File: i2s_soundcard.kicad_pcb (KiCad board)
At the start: 4 copper layers, 83.1 x 50 mm, 21 parts, among them J1 Conn_01x08, J2 Conn_01x06, J3 Conn_01x05, J4 Conn_01x11, J5 Conn_01x04, U1 TLV320AIC3104IRHBT, U2 FSA2275UMX, U3 TPA2006D1DRBR, U4 FSA2275UMX, U5 TPA2006D1DRBR, U6 TLV7111830DSER, U7 TPD4E02B04DQAR, U8 TPD4E02B04DQAR

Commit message: fill in rest of in2 with ground fill
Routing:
- net /vbat: track 25.9 -> 27.5 mm
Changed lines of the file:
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@@
     (thickness 1)
     (drawings 61)
-    (tracks 443)
+    (tracks 445)
     (zones 0)
     (modules 21)
@@
   (segment (start 159.054802 97.3) (end 161.954802 100.2) (width 0.19) (layer In2.Cu) (net 33))
   (segment (start 158.8 97.3) (end 159.054802 97.3) (width 0.19) (layer In2.Cu) (net 33))
+  (segment (start 166.2 100.2) (end 167.6 100.2) (width 0.19) (layer In2.Cu) (net 33))
+  (segment (start 167.6 100.2) (end 167.7 100.1) (width 0.19) (layer In2.Cu) (net 33))
   (segment (start 165.027989 100.027989) (end 166.2 101.2) (width 0.19) (layer F.Cu) (net 34))
   (segment (start 165.027989 96.585908) (end 165.027989 100.027989) (width 0.19) (layer F.Cu) (net 34))
@@
     (polygon
       (pts
-        (xy 173.275 76.6) (xy 169 80.875) (xy 168.5 106.9) (xy 164.5 106.2) (xy 164.3375 94.7375)
-        (xy 165.6 82.1) (xy 166.4 81.2) (xy 167.3 73.3) (xy 164.3 70.1) (xy 161.3 77.8)
-        (xy 103.3875 77.8) (xy 86.1 72.3) (xy 86.15 56) (xy 173.275 56)
+        (xy 173.275 76.6) (xy 169 80.875) (xy 168.509375 100.5) (xy 166.290625 100.45) (xy 166.3 95)
+        (xy 166.7 87) (xy 165.7 86.2) (xy 165.6 82.1) (xy 166.4 81.2) (xy 167.3 73.3)
+        (xy 164.3 70.1) (xy 161.3 77.8) (xy 103.3875 77.8) (xy 86.1 72.3) (xy 86.15 56)
+        (xy 173.275 56)
       )
     )
@@
     (polygon
       (pts
-        (xy 164.4 70.5) (xy 167 73.4) (xy 166.2 81) (xy 160.65 87.35) (xy 160.2 90.7)
-        (xy 161.3 93.6) (xy 161.3 95.4) (xy 159.35 95.4) (xy 159.5 95.9) (xy 157.7 94.1)
-        (xy 158.9 85.8) (xy 164.3 80.3) (xy 163.4 73)
+        (xy 164.4 70.5) (xy 167 73.4) (xy 166.2 81) (xy 165.3 82) (xy 165.5 86.3)
+        (xy 166.4 87.2) (xy 166 95.7) (xy 166 100.7) (xy 168.6 100.9) (xy 171.575 111.2)
+        (xy 153.4 108.7875) (xy 152.9 84.125) (xy 162.3 78.05) (xy 163.4 73)
       )
     )

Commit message: Capitalize net names
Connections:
- net /LOL+ renamed /LOL_P
- net /LOL- renamed /LOL_N
- net /LOR+ renamed /LOR_P
- net /LOR- renamed /LOR_N
- net /bclk renamed /BCLK
- net /din renamed /DIN
- net /dout renamed /DOUT
- net /en1 renamed /EN1
- net /en2 renamed /EN2
- net /intmic+ renamed /INTMIC_P
- net /intmic- renamed /INTMIC_N
- net /iovdd renamed /IOVDD
- net /mclk renamed /MCLK
- net /mute renamed /MUTE
- net /reset renamed /RESET
- net /ring1 renamed /RING1
- net /ring2 renamed /RING2
- net /ring2_again renamed /RING2_AGAIN
- net /sca renamed /SCA
- net /scl renamed /SCL
- net /sel renamed /SEL
- net /sleeve renamed /SLEEVE
- net /tip renamed /TIP
- net /v1.8 renamed /VCC1.8
- net /v3.3 renamed /VCC3.3
- net /vbat renamed /VBAT_3.7
- net /wclk renamed /WCLK
- net /~shutdown renamed /~SHUTDOWN
- net Net-(J1-Pad7) renamed /DETECT?

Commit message: Lots of schematic cleanup and board tweaking
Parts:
- added C10: 10uF, Capacitor_SMD:C_0402_1005Metric, B.Cu at (163.7, 91.7)
- added C11: 100nF, Capacitor_SMD:C_0402_1005Metric, B.Cu at (165.7, 91.7)
- added C8: 0.1uF, Capacitor_SMD:C_0402_1005Metric, B.Cu at (161.5, 92.0)
- added C9: 220nF, Capacitor_SMD:C_0402_1005Metric, B.Cu at (162.3, 86.5)
- C4: value 1uF -> 10uF; moved to B.Cu
- C5: value 1uF -> 22uF; moved to B.Cu
- U6: moved to B.Cu
- moved J4 4.22 mm to (166.2, 103.1)
- moved U6 3.28 mm to (163.1, 94.0), turned to 180 degrees
- moved C2 2.08 mm to (156.3, 97.5), turned to 270 degrees
- moved C4 1.84 mm to (160.9, 90.0), turned to 270 degrees
- moved C5 1.58 mm to (160.9, 88.0)
- moved U8 0.76 mm to (164.0, 82.6)
- moved U2 0.50 mm to (158.0, 98.1), turned to 0 degrees
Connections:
- net /VCC3.3 renamed /VCC3.0
- J3 pad 3: /EN2 -> /EN1
- J3 pad 5: /EN1 -> /EN2
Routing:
- net /SEL: track 24.5 -> 16.9 mm
- net /MUTE: track 23.6 -> 17.0 mm
- net /RESET: track 22.5 -> 16.0 mm
- net /VBAT_3.7: track 27.5 -> 33.1 mm
- net /spkr_amp_left/SLO+: track 96.6 -> 91.2 mm
- net /SCA: track 17.9 -> 12.7 mm
- net /SCL: track 16.8 -> 12.0 mm
- net /~SHUTDOWN: track 106.9 -> 102.5 mm
- net /DOUT: track 16.3 -> 11.9 mm
- net GND: track 47.8 -> 43.8 mm, vias 24 -> 23
- net /EN2: track 4.26 -> 8.18 mm
- net /DIN: track 16.1 -> 12.2 mm
- net /LOR_N: track 2.64 -> 6.43 mm
- net /VCC1.8: track 7.85 -> 4.22 mm, vias 2 -> 1
- net /WCLK: track 15.9 -> 12.6 mm
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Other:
- board size 83.1 x 50 mm -> 83.1 x 46.3 mm

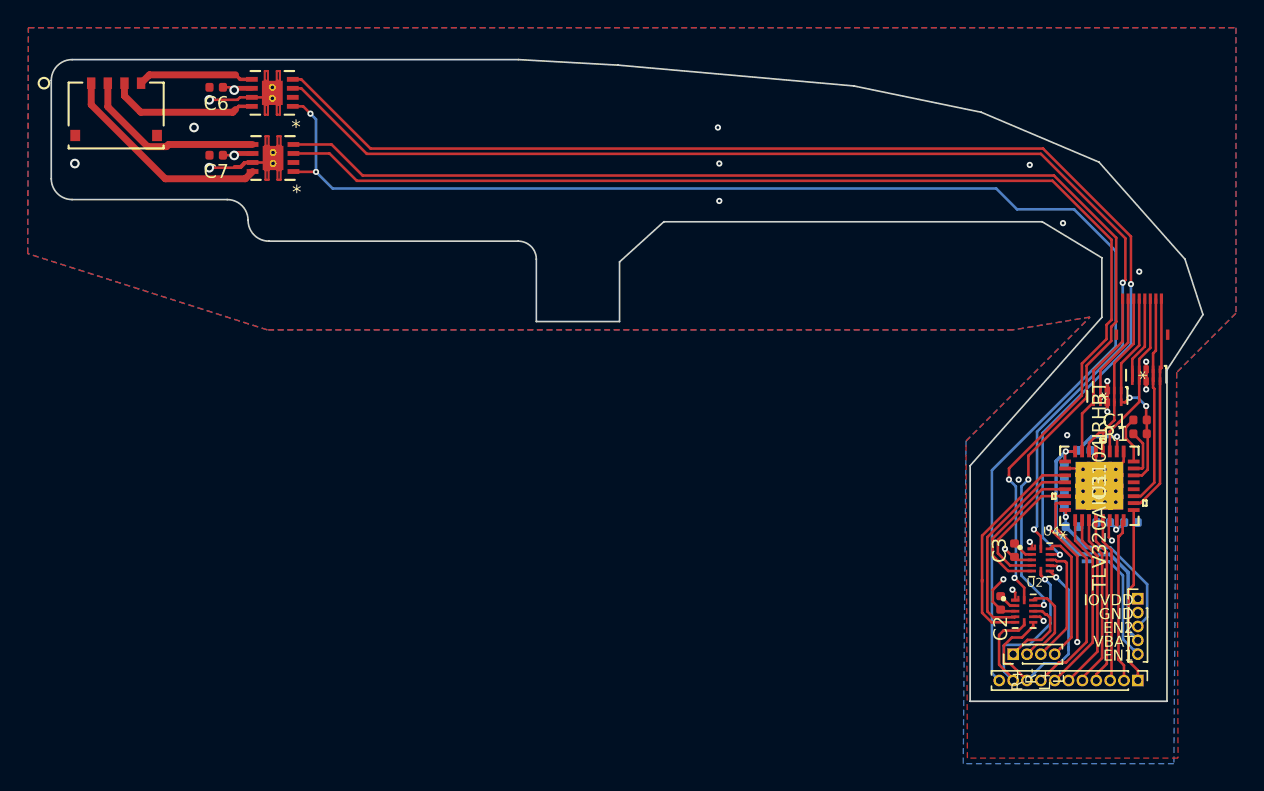
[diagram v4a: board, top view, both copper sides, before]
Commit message: AC-couple headphone outputs. This frees up HPRCOM and HPLCOM, which I can use for line outputs, since the dock line out is single-ended anyway.
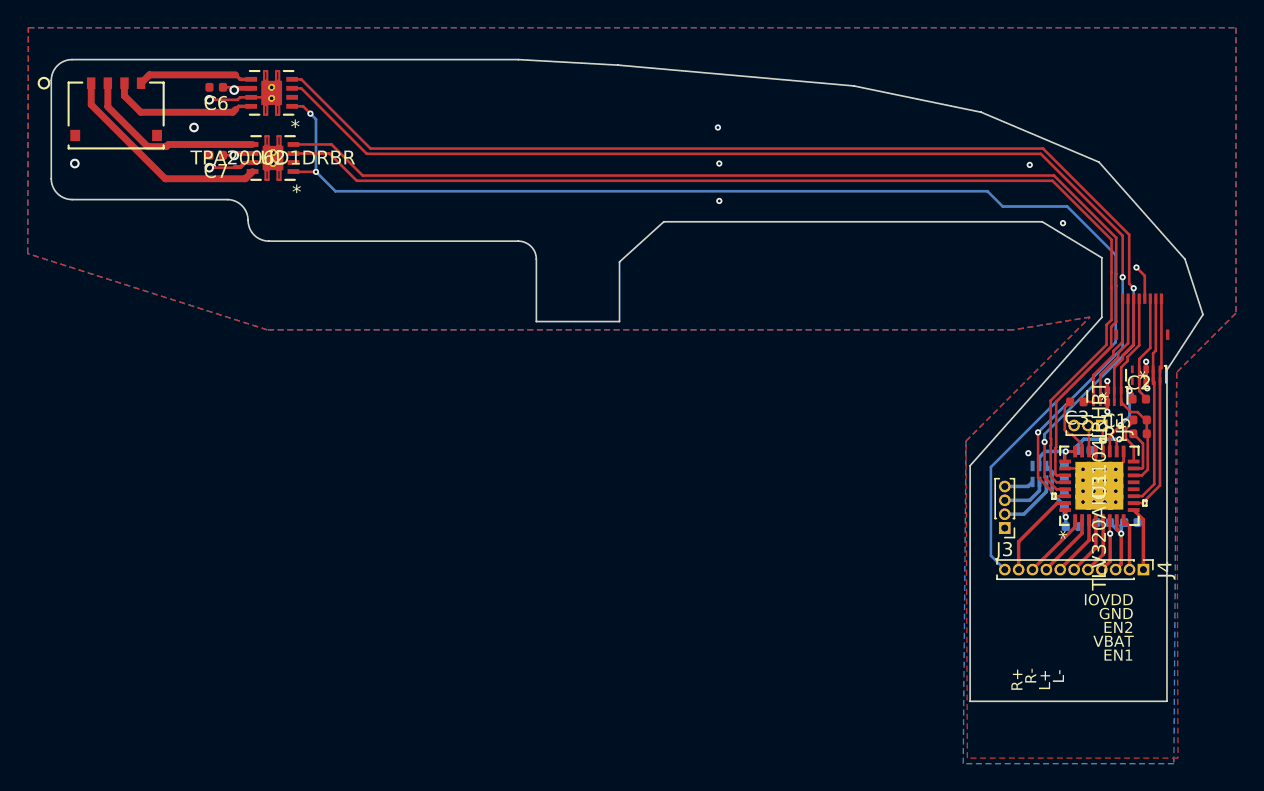
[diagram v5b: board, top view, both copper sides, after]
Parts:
- removed U4: FSA2275UMX, footprints:FSA2275
- removed U5: TPA2006D1DRBR, footprints:TPA2006D1DRBR
- C2, C3: value 0.1uF -> C
- J3: value Conn_01x05 -> Conn_01x04; footprint Connector_PinHeader_1.00mm:PinHeader_1x05_P1.00mm_Vertical -> Connector_PinHeader_1.00mm:PinHeader_1x04_P1.00mm_Vertical
- J5: value Conn_01x04 -> Conn_01x03; footprint Connector_PinHeader_1.00mm:PinHeader_1x04_P1.00mm_Vertical -> Connector_PinHeader_1.00mm:PinHeader_1x03_P1.00mm_Vertical
- U2: value FSA2275UMX -> TPA2006D1DRBR; footprint footprints:FSA2275 -> footprints:TPA2006D1DRBR
- moved U2 63.3 mm to (103.8, 65.4), turned to 180 degrees
- moved C2 17.8 mm to (166.3, 82.8), turned to 0 degrees
- moved J5 17.7 mm to (163.6, 84.7), turned to 270 degrees
- moved C3 11.6 mm to (161.8, 83.0), turned to 180 degrees
- moved J3 10.9 mm to (156.6, 92.1), turned to 180 degrees
- moved J4 8.01 mm to (166.6, 95.1)
- moved U6 7.05 mm to (159.1, 88.2), turned to 90 degrees
- moved U3 4.70 mm to (103.7, 60.7)
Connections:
- C2 pad 2: GND -> /TIP
- C3 pad 1: Net-(C3-Pad1) -> /RING1
- C3 pad 2: GND -> Net-(C3-Pad2)
- J1 pad 4: /RING2 -> GND
- J3 pad 1: /IOVDD -> GND
- J3 pad 2: GND -> /EN1
- J3 pad 3: /EN1 -> /VBAT_3.7
- J3 pad 4: /VBAT_3.7 -> /EN2
- J4 pad 10: /SEL -> /RESET
- J4 pad 3: /DOUT -> /IOVDD
- J4 pad 4: /DIN -> GND
- J4 pad 5: /WCLK -> /DOUT
- J4 pad 6: /BCLK -> /DIN
- J4 pad 7: /MCLK -> /WCLK
- J4 pad 8: /RESET -> /BCLK
- J4 pad 9: /MUTE -> /MCLK
- J5 pad 1: /LOR_P -> /LOL
- J5 pad 2: /LOR_N -> /LOR
- J5 pad 3: /LOL_P -> GND
- U1 pad 12: Net-(U1-Pad12) -> (no net)
- U1 pad 13: Net-(U1-Pad13) -> (no net)
- U1 pad 19: /TIP -> Net-(C2-Pad1)
- U1 pad 20: /RING2_AGAIN -> /LOL
- U1 pad 22: /RING2_AGAIN -> /LOR
- U1 pad 23: /RING1 -> Net-(C3-Pad2)
- U2 pad 1: /VBAT_3.7 -> /~SHUTDOWN
- U2 pad 2: Net-(C2-Pad1) -> (no net)
- U2 pad 3: GND -> /spkr_amp_left/LINEIN-
- U2 pad 4: /spkr_amp_left/LINEIN- -> /spkr_amp_left/LINEIN+
- U2 pad 5: /spkr_amp_left/LINEIN+ -> /spkr_amp_left/SPKR-
- U2 pad 6: /SEL -> /VBAT_3.7
- U2 pad 7: /MUTE -> GND
- U2 pad 8: GND -> /spkr_amp_left/SPKR+
- U2 pad 9: /LOR_P -> GND
- U3 pad 2: Net-(U3-Pad2) -> (no net)
- U3 pad 3: /spkr_amp_left/SLO+ -> /spkr_amp_right/LINEIN-
- U3 pad 4: /spkr_amp_left/SLO- -> /spkr_amp_right/LINEIN+
- U3 pad 5: /spkr_amp_left/SPKR- -> /spkr_amp_right/SPKR-
- U3 pad 8: /spkr_amp_left/SPKR+ -> /spkr_amp_right/SPKR+
- U7 pad 5: /RING2 -> (no net)
- U7 pad 6: /RING2 -> (no net)
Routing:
- net /spkr_amp_left/SLO-: track 92.9 -> 0.00 mm, vias 2 -> 0
- net /spkr_amp_right/SLO-: track 92.0 -> 0.00 mm, vias 2 -> 0
- net /spkr_amp_left/SLO+: track 91.2 -> 0.00 mm, vias 2 -> 0
- net /spkr_amp_right/SLO+: track 89.9 -> 0.00 mm, vias 2 -> 0
- net /spkr_amp_right/LINEIN-: track 9.93 -> 86.8 mm, vias 0 -> 2
- net /spkr_amp_right/LINEIN+: track 11.2 -> 87.1 mm, vias 0 -> 2
- net /spkr_amp_left/LINEIN-: track 14.8 -> 81.7 mm
- net /spkr_amp_left/LINEIN+: track 16.2 -> 81.8 mm
- net /VBAT_3.7: track 33.1 -> 7.85 mm, vias 4 -> 2
- net /MUTE: track 17.0 -> 0.00 mm, vias 1 -> 0
- net /SEL: track 16.9 -> 0.00 mm, vias 1 -> 0
- net GND: track 43.8 -> 33.3 mm, vias 23 -> 16
- net /RESET: track 16.0 -> 6.52 mm
- net /LOL_N: track 9.49 -> 0.00 mm
- net /LOL_P: track 8.67 -> 0.00 mm
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
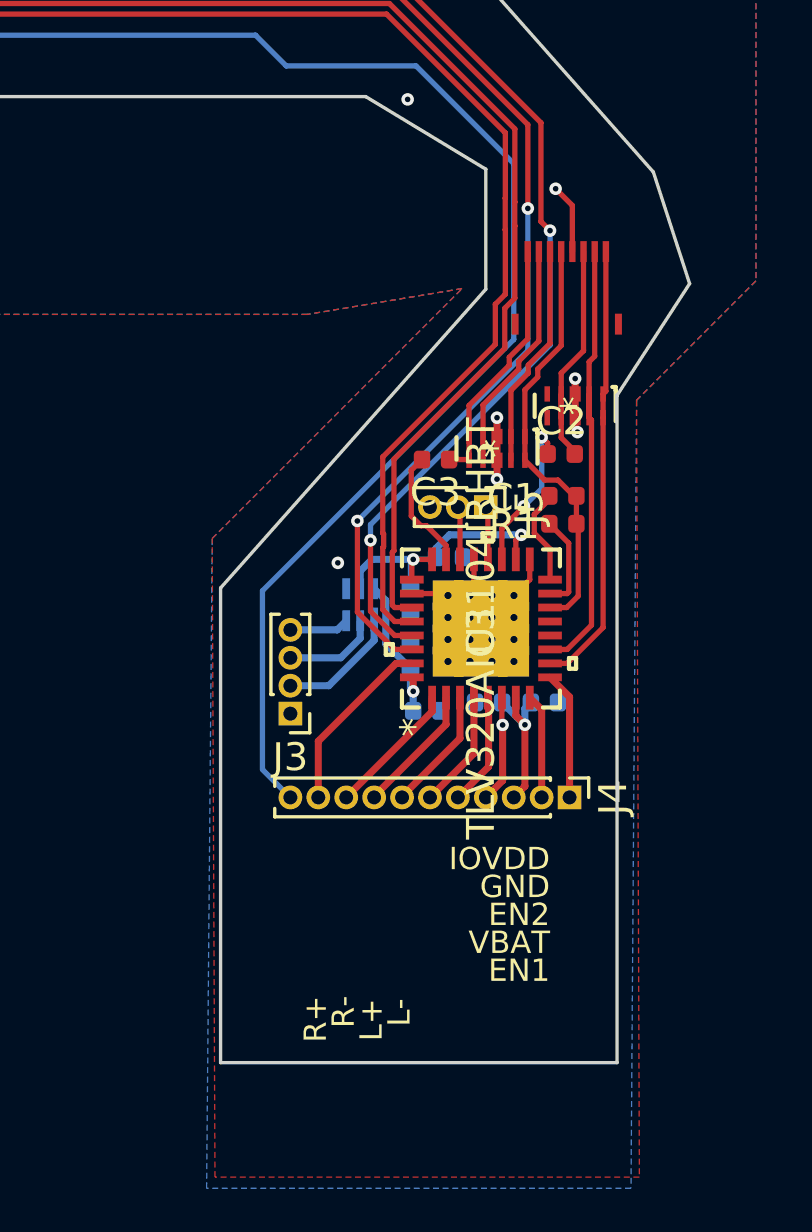
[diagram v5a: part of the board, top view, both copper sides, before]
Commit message: Shrink board
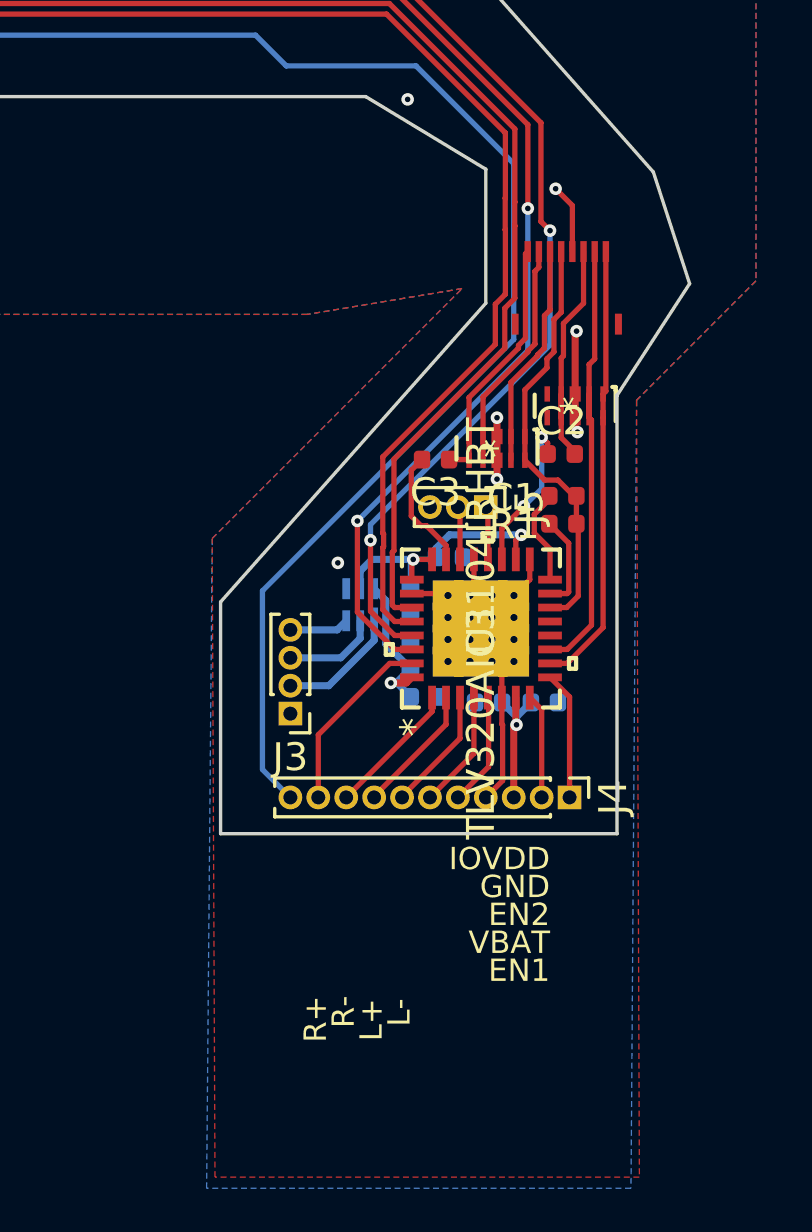
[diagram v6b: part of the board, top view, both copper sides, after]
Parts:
- moved C8 0.51 mm to (161.4, 91.5)
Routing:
- net GND: track 33.3 -> 36.5 mm, vias 16 -> 15
- net /VCC1.8: track 5.48 -> 6.07 mm
- net /IOVDD: track 6.19 -> 5.65 mm
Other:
- board size 83.1 x 46.3 mm -> 83.1 x 38.1 mm

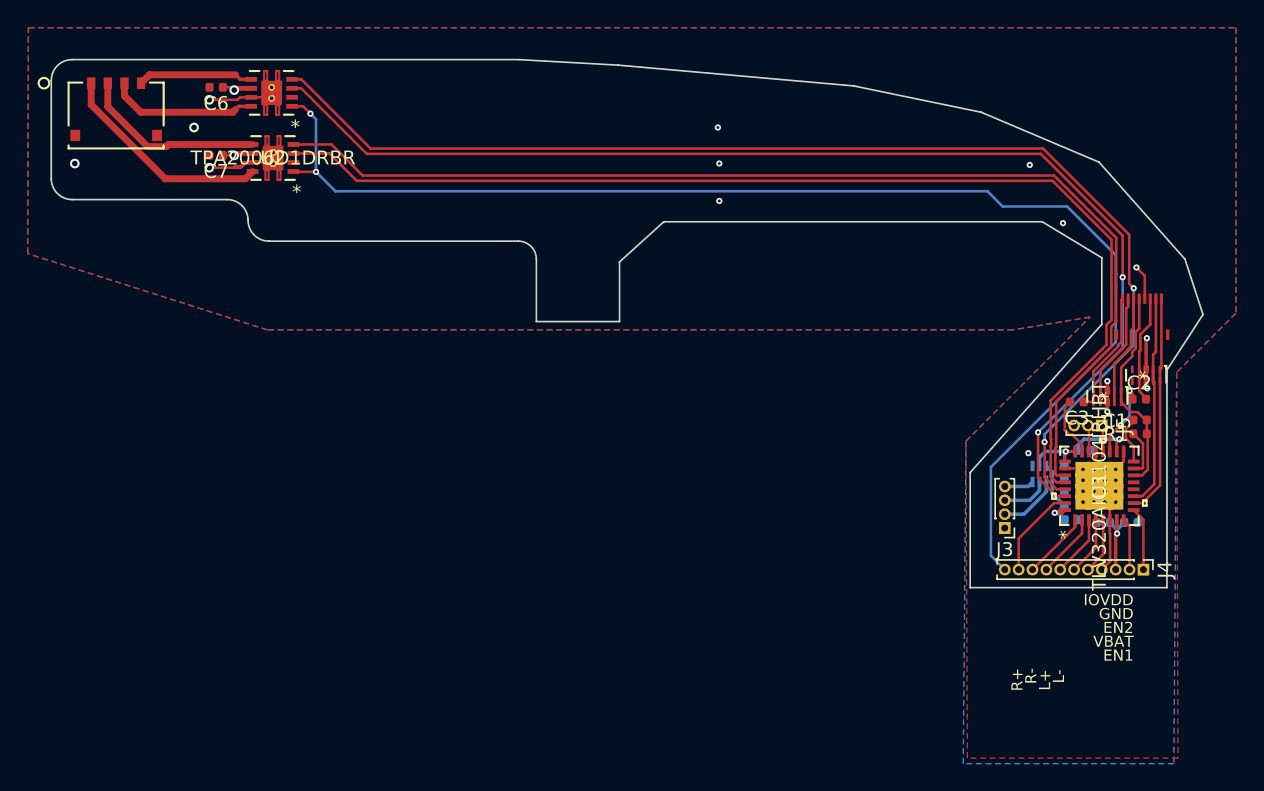
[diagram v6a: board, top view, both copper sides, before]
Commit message: Clean up silkscreen a bit
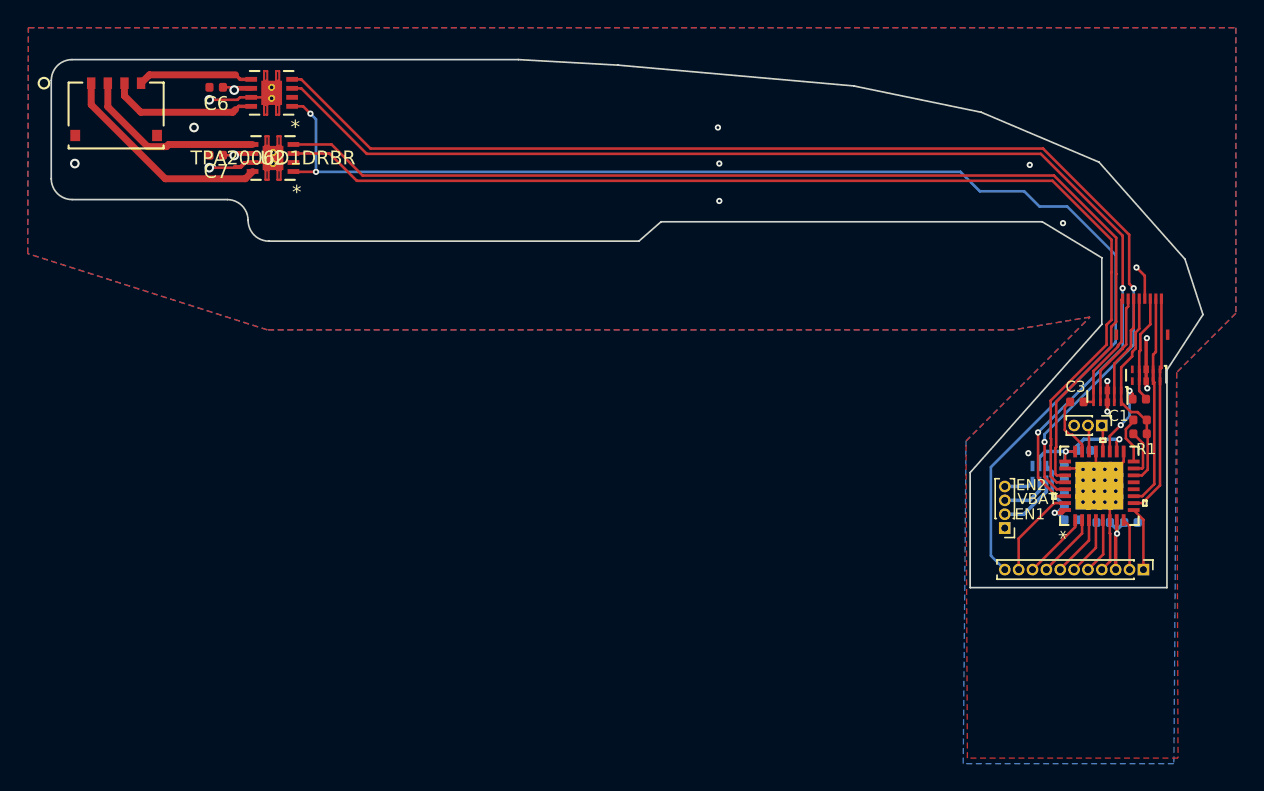
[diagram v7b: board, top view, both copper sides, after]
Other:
- outline, holes or cut-outs redrawn
- board text added: "DO"
- board text removed: "DOUT"
- board text removed: "L+"
- board text removed: "L-"
- board text removed: "MUTE"
- board text removed: "R+"
- board text removed: "R-"
- board text removed: "SEL"
